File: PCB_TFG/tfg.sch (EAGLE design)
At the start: 11 parts, among them T1 2N2222

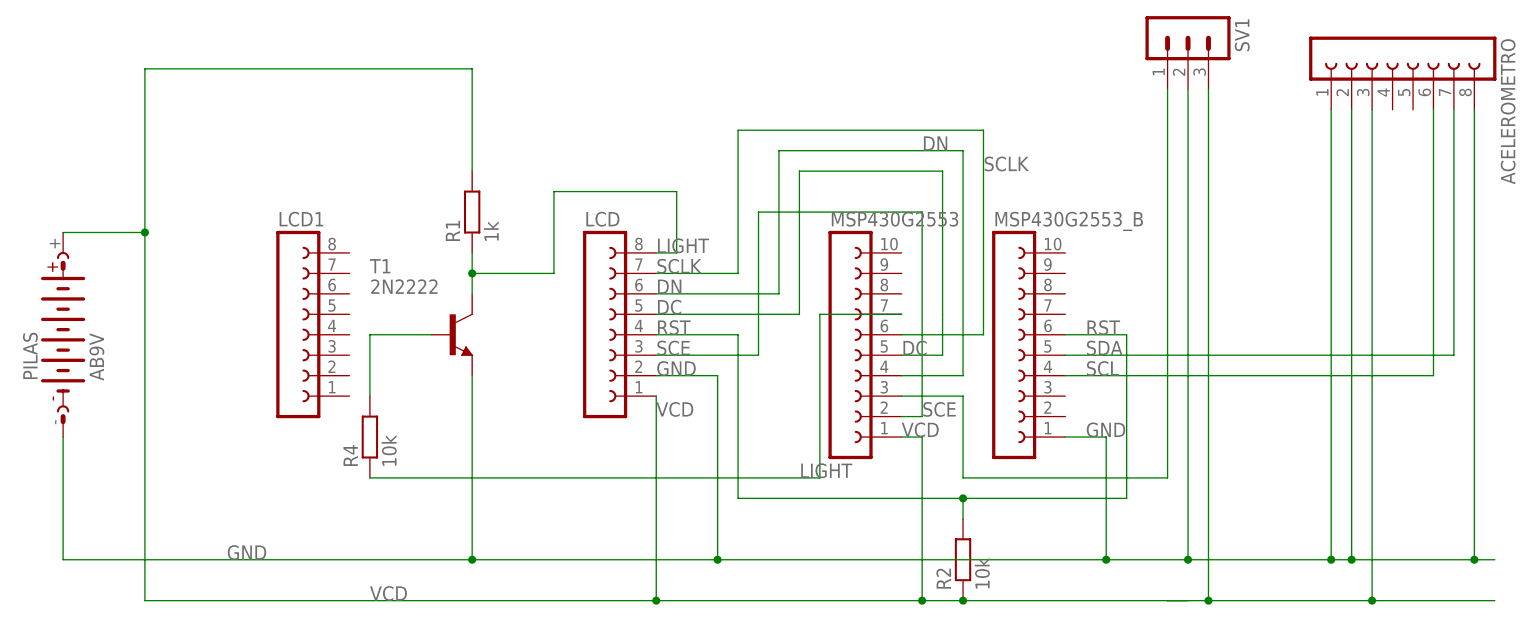
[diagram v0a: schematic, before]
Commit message: schematic modified
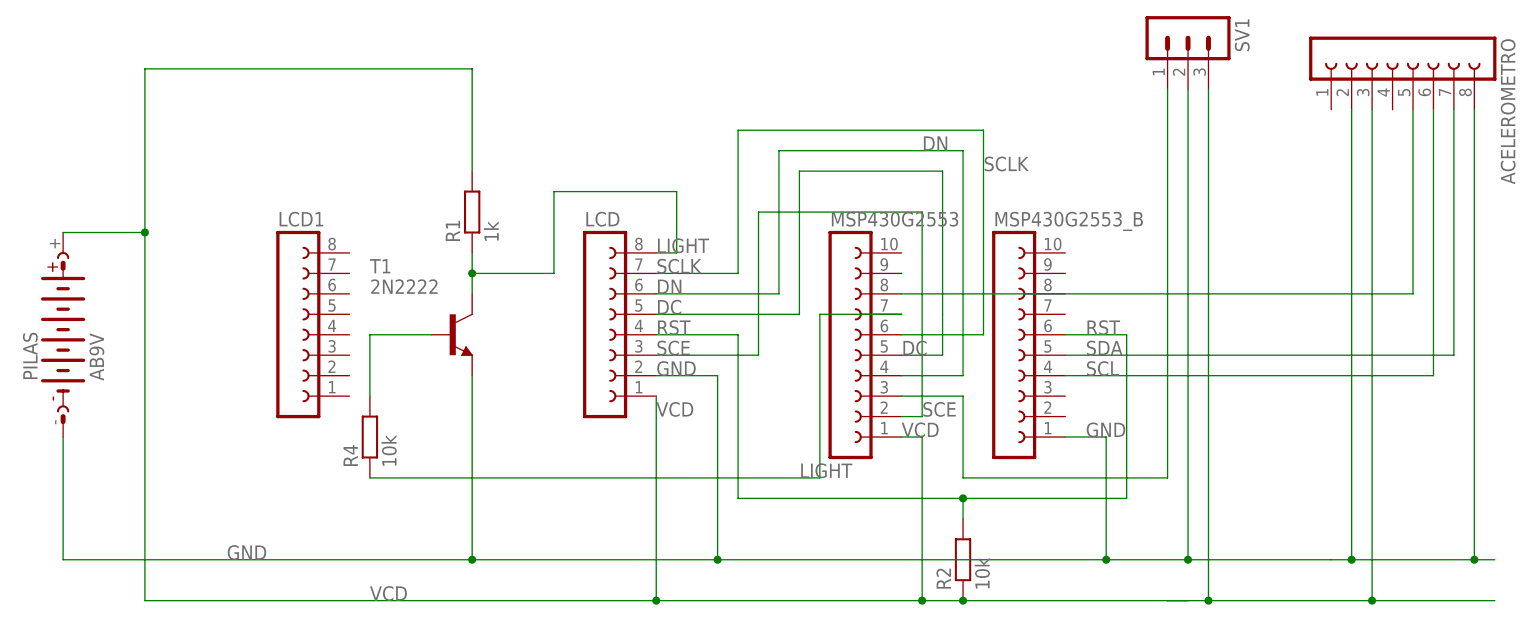
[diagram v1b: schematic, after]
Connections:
- new net N$4: ACELEROMETRO.5, MSP430G2553.8
- net GND: no longer ACELEROMETRO.1
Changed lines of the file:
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@@
 <wire x1="149.86" y1="68.58" x2="149.86" y2="12.7" width="0.1524" layer="91"/>
 <junction x="149.86" y="12.7"/>
-<pinref part="ACELEROMETRO" gate="G$1" pin="1"/>
-<wire x1="147.32" y1="68.58" x2="147.32" y2="12.7" width="0.1524" layer="91"/>
-<junction x="147.32" y="12.7"/>
 <label x="10.16" y="12.7" size="1.778" layer="95"/>
 <label x="63.5" y="35.56" size="1.778" layer="95"/>
@@
 </segment>
 </net>
+<net name="N$4" class="0">
+<segment>
+<pinref part="MSP430G2553" gate="G$1" pin="8"/>
+<pinref part="ACELEROMETRO" gate="G$1" pin="5"/>
+<wire x1="93.98" y1="45.72" x2="157.48" y2="45.72" width="0.1524" layer="91"/>
+<wire x1="157.48" y1="45.72" x2="157.48" y2="68.58" width="0.1524" layer="91"/>
+</segment>
+</net>
